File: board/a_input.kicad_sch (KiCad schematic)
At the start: 13 parts

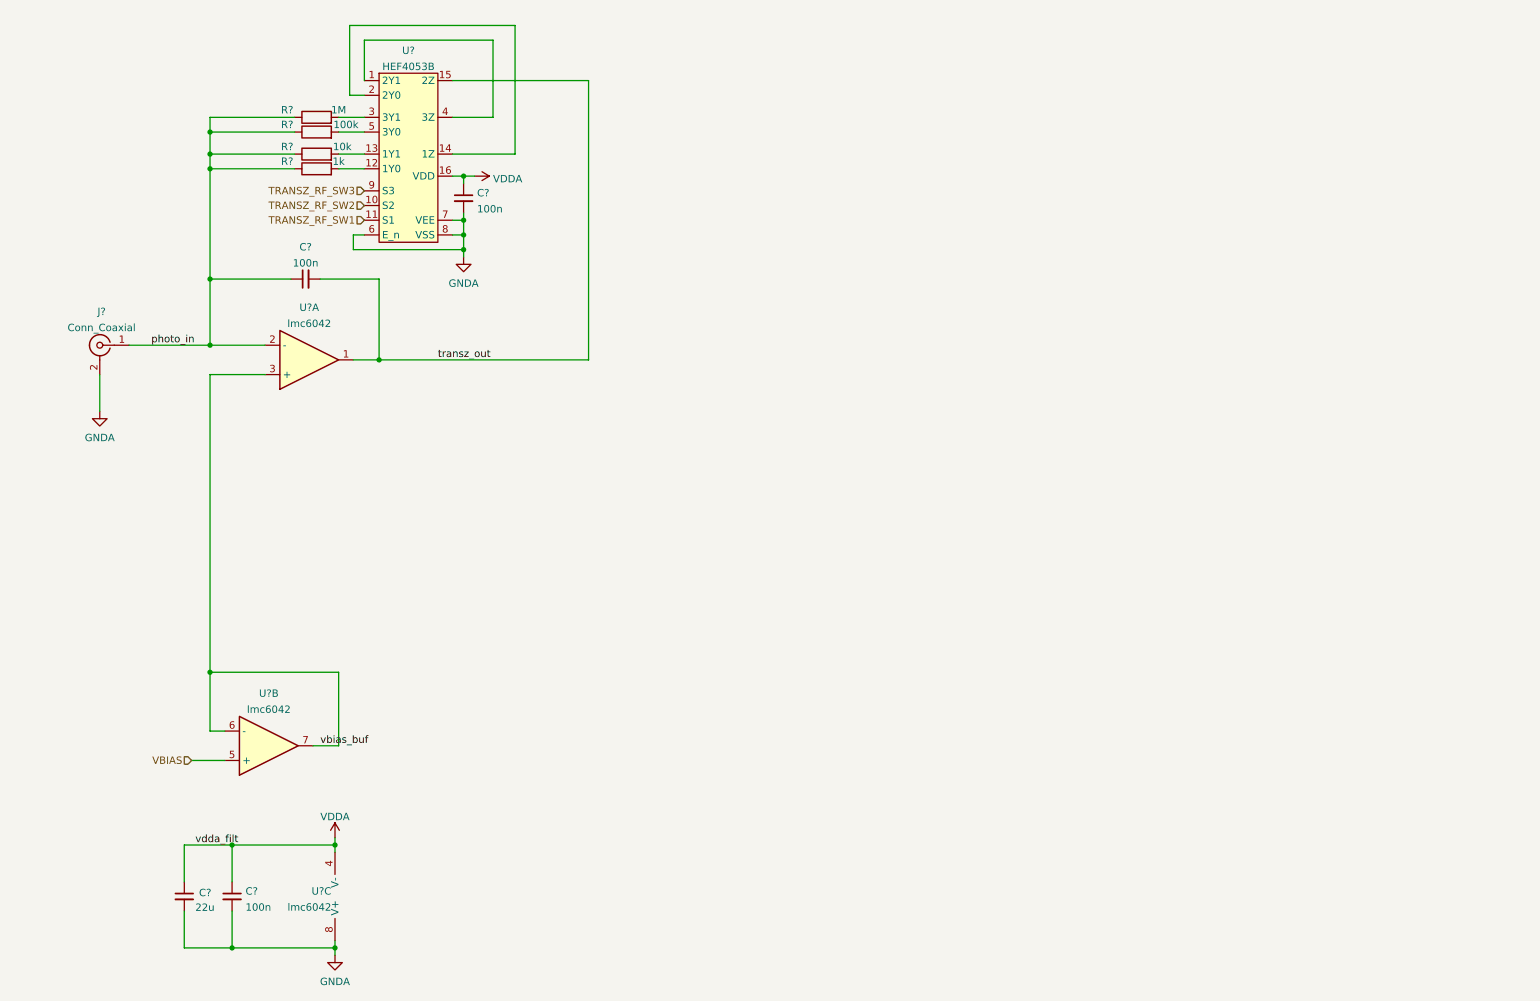
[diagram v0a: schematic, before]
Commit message: Finalize input tranz amp, to diff, protection
layout left
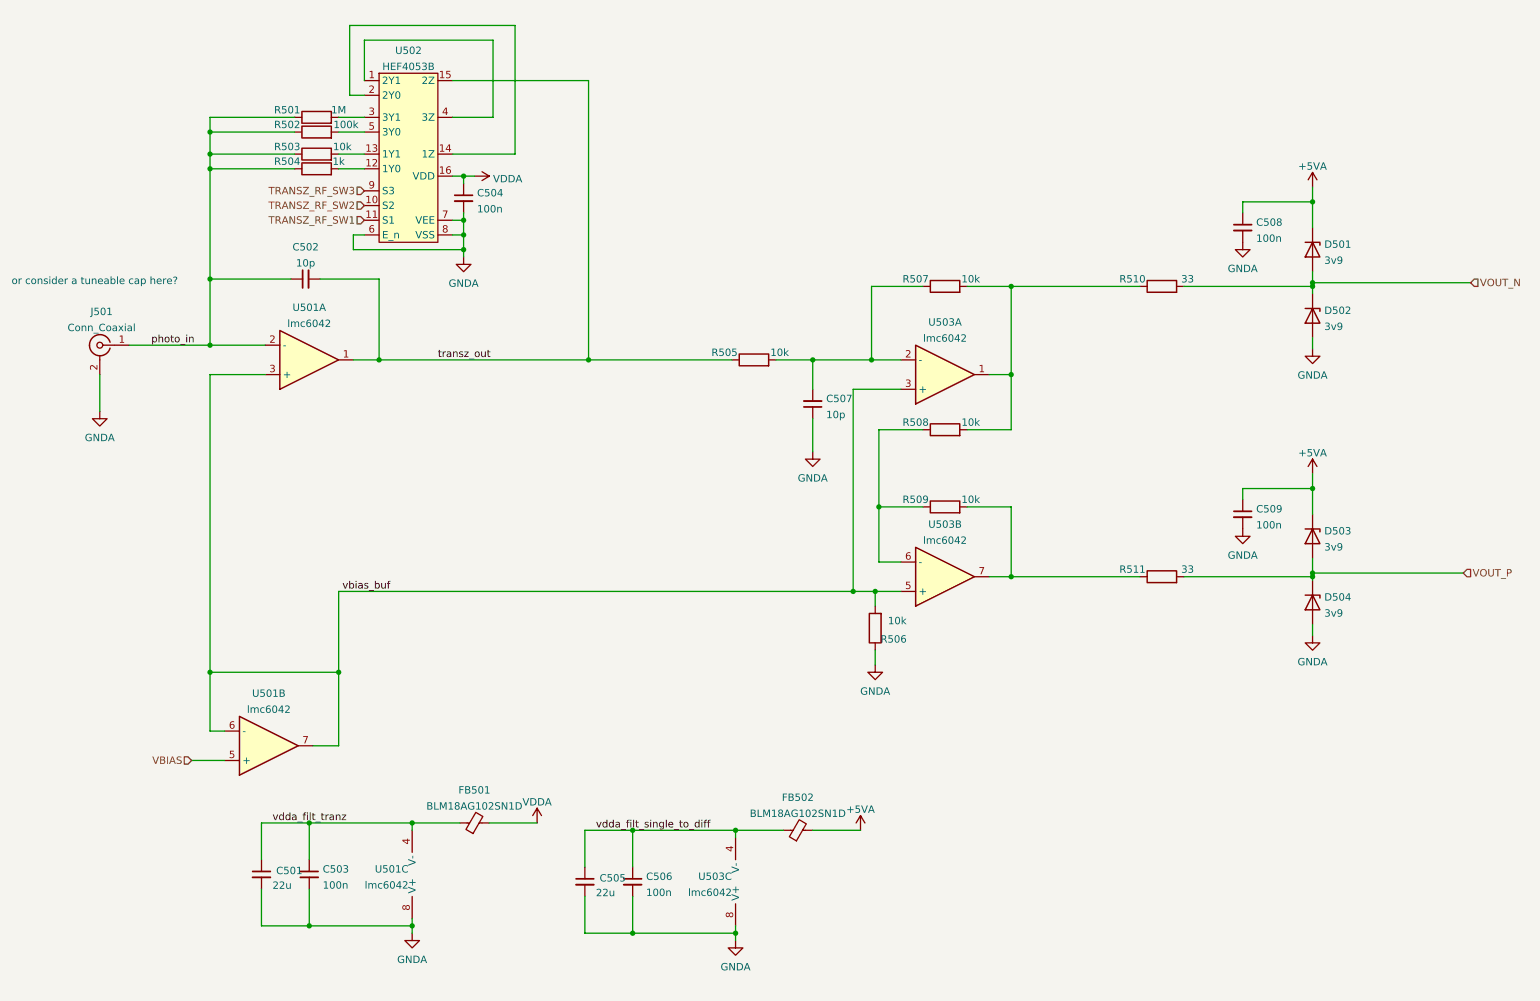
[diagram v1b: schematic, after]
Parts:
- added C505: 22u, Capacitor_SMD:C_0603_1608Metric_Pad1.08x0.95mm_HandSolder, symbol Device:C_Small
- added C506, C508, C509: 100n, Capacitor_SMD:C_0603_1608Metric_Pad1.08x0.95mm_HandSolder, symbol Device:C_Small
- added C507: 10p, Capacitor_SMD:C_0603_1608Metric_Pad1.08x0.95mm_HandSolder, symbol Device:C_Small
- added D501, D502, D503, D504: 3v9, Diode_THT:D_DO-41_SOD81_P2.54mm_Vertical_AnodeUp, symbol Device:D_Zener
- added FB501, FB502: BLM18AG102SN1D, Inductor_SMD:L_0603_1608Metric_Pad1.05x0.95mm_HandSolder, symbol Device:FerriteBead_Small
- added R505, R506, R507, R508, R509: 10k, Resistor_SMD:R_0603_1608Metric_Pad0.98x0.95mm_HandSolder, symbol Device:R
- added R510, R511: 33, Resistor_SMD:R_0603_1608Metric_Pad0.98x0.95mm_HandSolder, symbol Device:R
- added U503: lmc6042, Package_SO:SOIC-8_3.9x4.9mm_P1.27mm, symbol Device:Opamp_Dual
- C502: renamed from C?; value 100n -> 10p
- gave numbers to parts that had none: 10
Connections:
- net GNDA: now also C505.2, C506.2, C507.1, C508.2, C509.2, D502.2 (A), D504.2 (A), R506.1, U503.8 (V+)
- net VDDA: now also FB501.2; no longer C501.1, C503.1, U501.4 (V-)
- net transz_out: now also R505.1
- net vbias_buf: now also R506.2, U503.3 (+), U503.5 (+)
- new net: R509.2, R511.1, U503.7
- new net: R508.1, R509.1, U503.6 (-)
- new net: R507.2, R508.2, R510.1, U503.1
- new net: C507.2, R505.2, R507.1, U503.2 (-)
- new net +5VA: C508.1, C509.1, D501.1 (K), D503.1 (K), FB502.2
- new net VOUT_N: D501.2 (A), D502.1 (K), R510.2
- new net VOUT_P: D503.2 (A), D504.1 (K), R511.2
- new net vdda_filt_single_to_diff: C505.1, C506.1, FB502.1, U503.4 (V-)
- new net vdda_filt_tranz: C501.1, C503.1, FB501.1, U501.4 (V-)
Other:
- note added: "or consider a tuneable cap here?"
- moved on the sheet: C501, C503, U501C

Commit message: some pcb digital moved
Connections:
- net transz_out: now also U502.14 (1Z); no longer U502.15 (2Z)
- net at R503.2: now also U502.1 (2Y1); no longer U502.13 (1Y1)
- net vout_p_prer: now reaches R509.2, R511.1, U503.7
- net single_2_diff_fb: now reaches R508.1, R509.1, U503.6 (-)
- net vout_n_prer: now reaches R507.2, R508.2, R510.1, U503.1
- net transz_filtered: now reaches C507.2, R505.2, R507.1, U503.2 (-)
- net at U502.4 (3Z): now also U502.12 (1Y0); no longer U502.1 (2Y1)
- net at R504.2: now also U502.2 (2Y0); no longer U502.12 (1Y0)
- new net: U502.13 (1Y1), U502.15 (2Z)
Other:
- moved on the sheet: R503, R504, R505

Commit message: pcb done
attempt at doing some sw. builds but not tested
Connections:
- net transz_x1: now reaches U502.12 (1Y0), U502.4 (3Z)
- net transz_x2: now reaches U502.13 (1Y1), U502.15 (2Z)
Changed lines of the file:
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@@
+    (effects (font (size 1.27 1.27)) (justify left bottom))
+  )
+  (label "transz_x2" (at 83.82 36.195 0)
     (effects (font (size 1.27 1.27)) (justify left bottom))
   )
@@
     (effects (font (size 1.27 1.27)) (justify left bottom))
   )
+  (label "transz_x1" (at 83.82 33.655 0)
+    (effects (font (size 1.27 1.27)) (justify left bottom))
+  )
